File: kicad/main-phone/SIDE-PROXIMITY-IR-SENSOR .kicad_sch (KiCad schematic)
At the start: 1 part

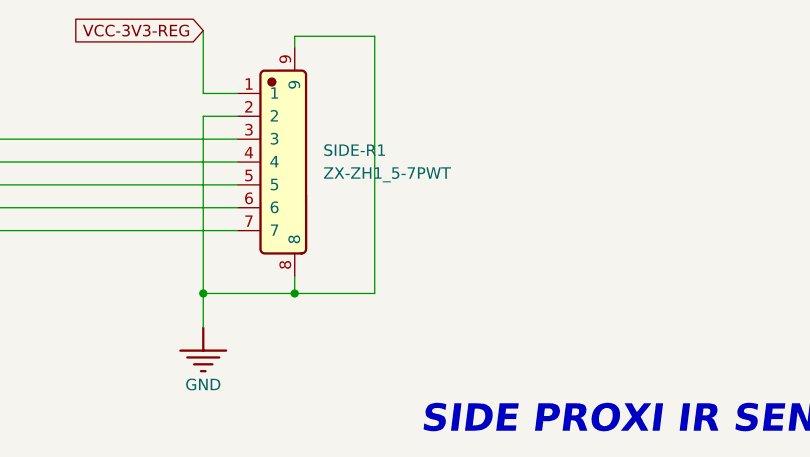
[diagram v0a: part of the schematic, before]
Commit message: Side sensor board rev 2 (VL53L0X + IRM-H638T, JST SH); mounting holes on dock and sensor boards
- kicad/side-sensors: VL53L0X (C91199) replaces the NRND VL6180 and its 2.8 V LDO;
  top-looking IRM-H638T replaces the TSOP38238; ZX-SH1.0-7PWT connector, same pinout;
  10k XSHUT/GPIO1 pull-ups, no local I2C pull-ups; refs 84xx; libs from ../main
- main-phone SIDE-R1: ZX-ZH1.5-7PWT -> ZX-SH1.0-7PWT
- mounting holes: dock 4x M3 (H8201-H8204), ToF board 2x M2 (H8301/H8302),
  side board 2x M2 (H8401/H8402)
- JLCImport: VL53L0CXV0DH_1 symbol, footprint, 3D model
- docs: side board README, SPEC, READMEs; IRM-H638T pinout confirmed

Co-Authored-By: Claude Opus 5.5 (1M context) <noreply@anthropic.com>
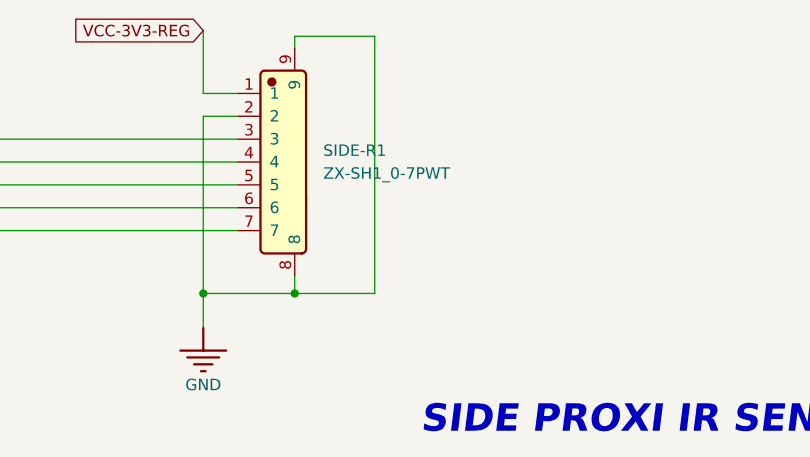
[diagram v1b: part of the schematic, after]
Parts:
- SIDE-R1: value ZX-ZH1_5-7PWT -> ZX-SH1_0-7PWT; footprint JLCImport:ZX-ZH1_5-7PWT -> JLCImport:ZX-SH1_0-7PWT; symbol JLCImport:ZX-ZH1_5-7PWT -> JLCImport:ZX-SH1_0-7PWT; LCSC C19272410 -> C7430449; Manufacturer Part ZX-ZH1.5-7PWT -> ZX-SH1.0-7PWT
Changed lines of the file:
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@@
 	)
 	(symbol
-		(lib_id "JLCImport:ZX-ZH1_5-7PWT")
+		(lib_id "JLCImport:ZX-SH1_0-7PWT")
 		(at 134.62 80.01 0)
 		(unit 1)
@@
 			)
 		)
-		(property "Value" "ZX-ZH1_5-7PWT"
+		(property "Value" "ZX-SH1_0-7PWT"
 			(at 139.065 81.2799 0)
 			(show_name no)
@@
 			)
 		)
-		(property "Footprint" "JLCImport:ZX-ZH1_5-7PWT"
+		(property "Footprint" "JLCImport:ZX-SH1_0-7PWT"
 			(at 134.62 80.01 0)
 			(hide yes)
@@
 			)
 		)
-		(property "Datasheet" "https://wmsc.lcsc.com/wmsc/upload/file/pdf/v2/lcsc/2312011606_Megastar-ZX-ZH1-5-7PWT_C19272410.pdf"
+		(property "Datasheet" "https://www.lcsc.com/datasheet/C7430449.pdf"
 			(at 134.62 80.01 0)
 			(hide yes)
@@
 			)
 		)
-		(property "Description" "-25℃~+85℃ 1 1.5mm 13.5mm 1A 1x7P 250V 3.8mm 6mm 7 7P Auxiliary Solder Pin Beige Brass LCP Surface Mount, Right Angle Tin ZH SMD,P=1.5mm,卧贴 Wire To Board Connector ROHS"
+		(property "Description" "JST SH compatible 1.0 mm 1x7P, SMD right angle; to the side sensor board (J8401)"
 			(at 134.62 80.01 0)
 			(hide yes)
@@
 			)
 		)
-		(property "LCSC" "C19272410"
+		(property "LCSC" "C7430449"
 			(at 134.62 80.01 0)
 			(hide yes)
@@
 			)
 		)
-		(property "Manufacturer Part" "ZX-ZH1.5-7PWT"
+		(property "Manufacturer Part" "ZX-SH1.0-7PWT"
 			(at 134.62 80.01 0)
 			(hide yes)

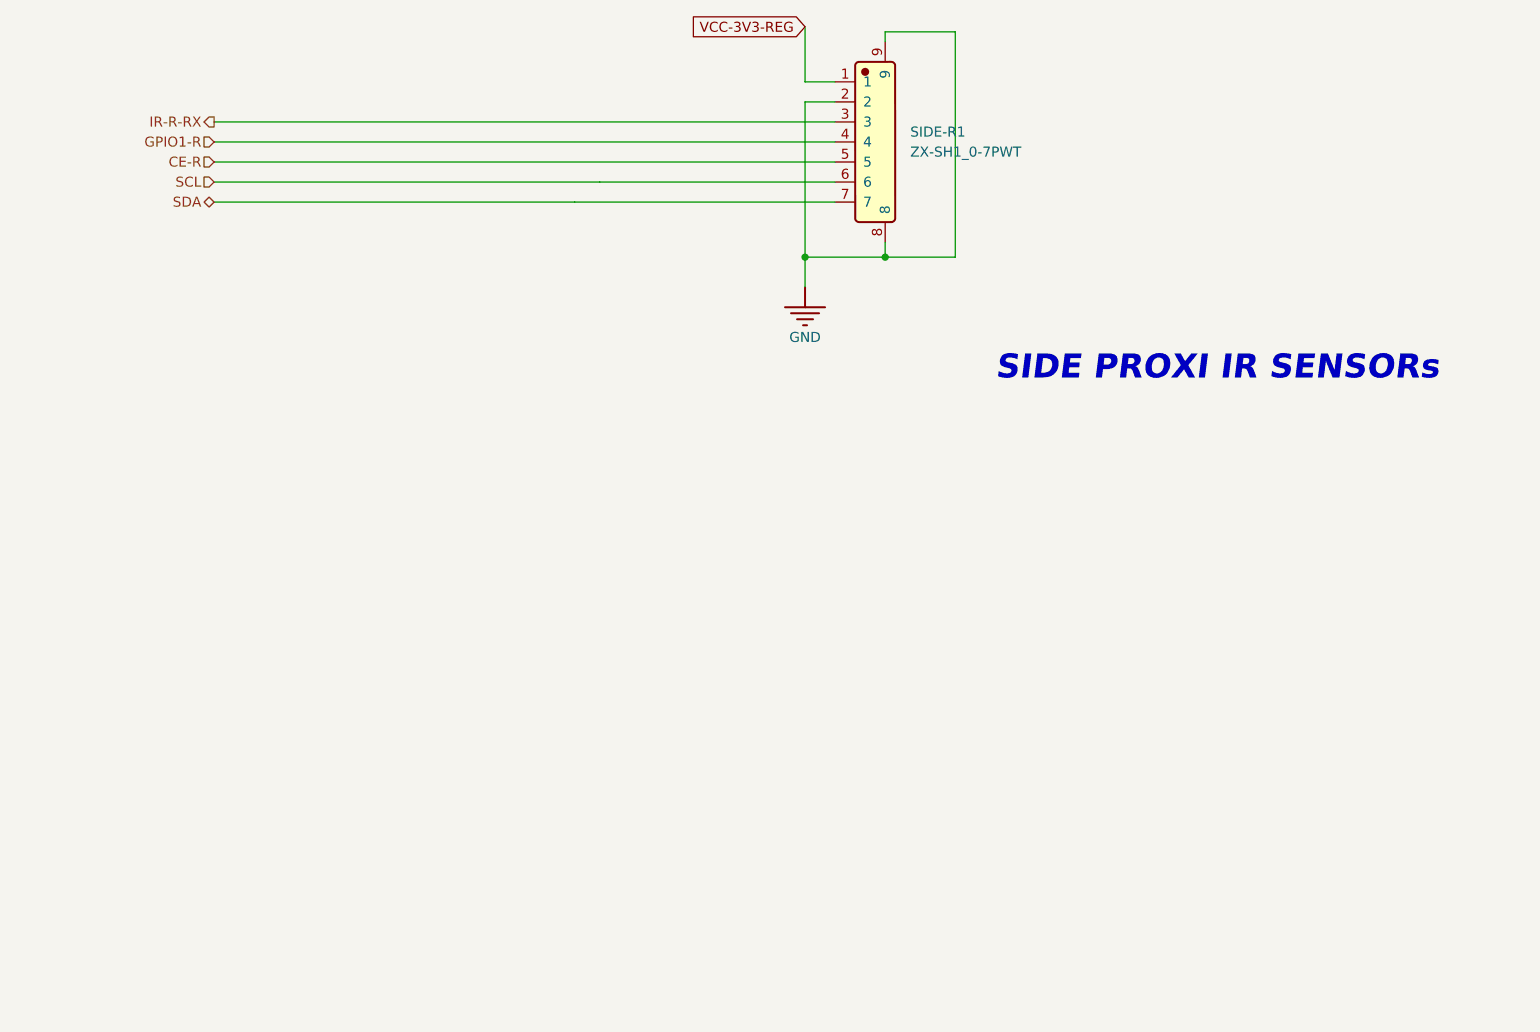
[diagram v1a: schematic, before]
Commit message: Rear docking IR board and Hall sensor board; main-board connectors
- kicad/rear-ir: 2x top-looking IRM-H638T with per-receiver 100R + 10uF filters, SH 4-pin
  vertical (3.3 V, IR_L, IR_R, GND), 2x M2. Refs 86xx.
- kicad/hall-sensor: CC6201ST omnipolar Hall switch + 100 nF, SH 4-pin vertical, 2x M2;
  fitted twice (dust bin, LiDAR tower bumper). Refs 87xx.
- main-phone SIDE-PROXI sheet: REAR-IR1 (PC8/PC9), HALL-BIN1 (PE4), HALL-TOWER1 (PE5),
  47k Hall pull-ups R7801/R7802; global labels to the MCU sheet; J7301 labels updated
- JLCImport: CC6201ST
- docs: board READMEs, SPEC, READMEs

Co-Authored-By: Claude Opus 5.5 <noreply@anthropic.com>
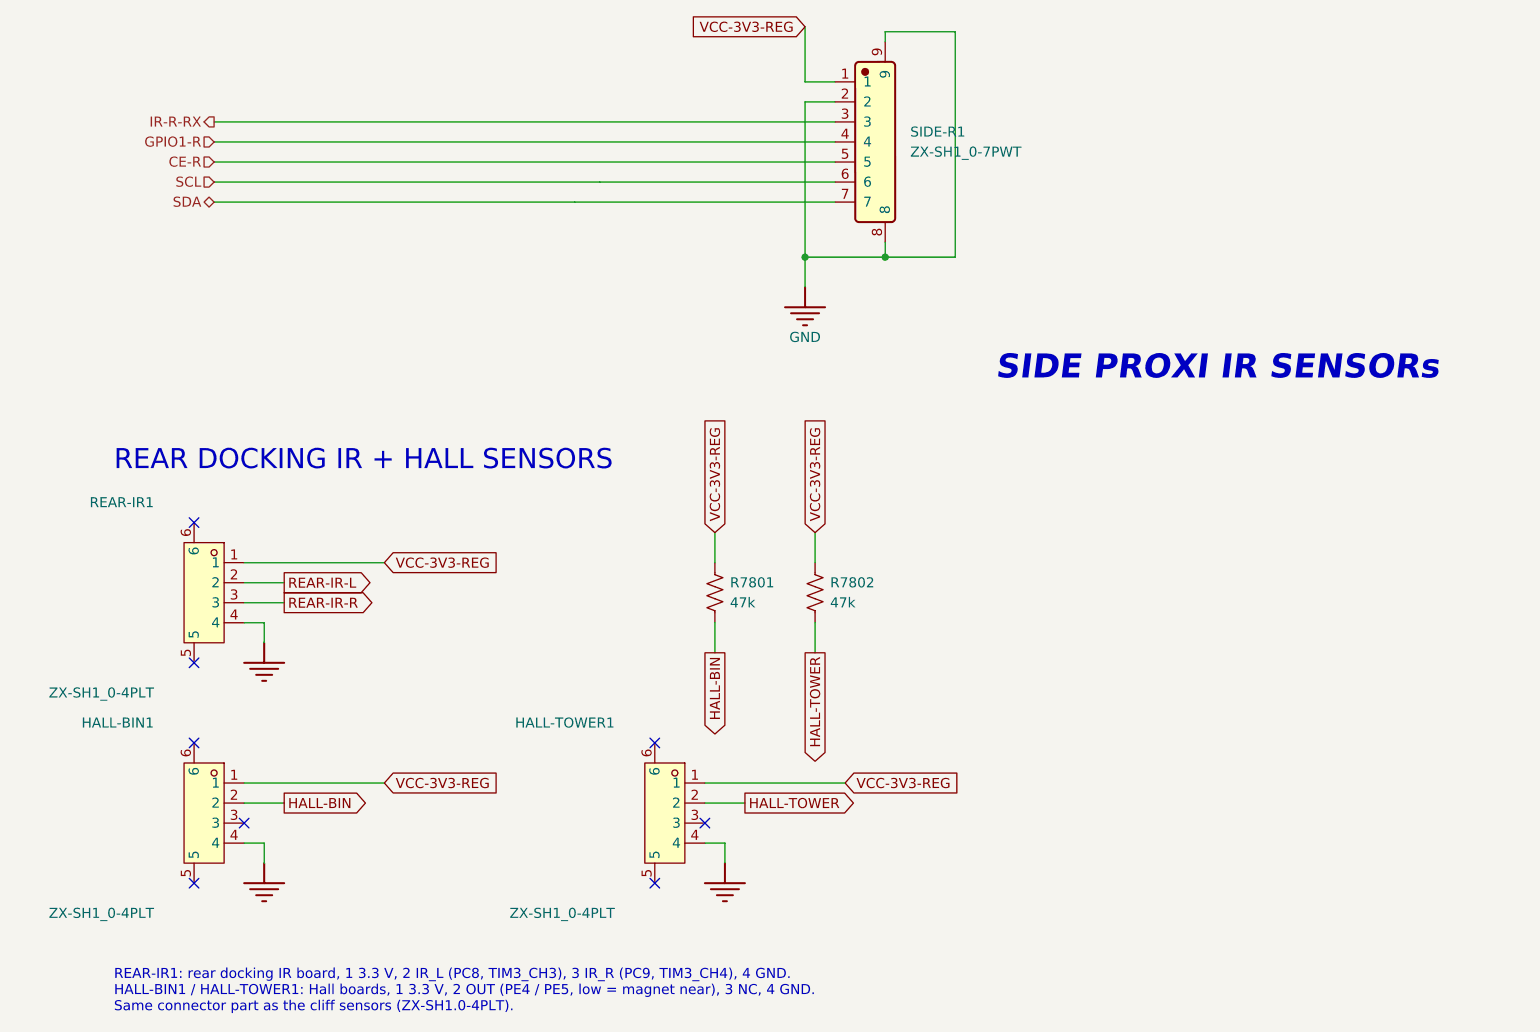
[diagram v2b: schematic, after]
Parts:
- added HALL-BIN1, HALL-TOWER1, REAR-IR1: ZX-SH1_0-4PLT, JLCImport:ZX-SH1_0-4PLT, symbol JLCImport:ZX-SH1_0-4PLT
- added R7801, R7802: 47k, Resistor_SMD:R_0603_1608Metric, symbol Device:R_US
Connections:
- net GND: now also HALL-BIN1.4, HALL-TOWER1.4, REAR-IR1.4
- net VCC-3V3-REG: now also HALL-BIN1.1, HALL-TOWER1.1, R7801.1, R7802.1, REAR-IR1.1
- new net HALL-BIN: HALL-BIN1.2, R7801.2
- new net HALL-TOWER: HALL-TOWER1.2, R7802.2
- new net REAR-IR-L: REAR-IR1.2
- new net REAR-IR-R: REAR-IR1.3
- no-connect marks 0 -> 8
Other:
- note added: "REAR DOCKING IR + HALL SENSORS"
- note added: "REAR-IR1: rear docking IR board, 1 3.3 V, 2 IR_L (PC8, TIM3_CH3), 3 IR_R (PC9, TIM3_CH4), 4 GND. HALL-BIN1 / HALL-TOWER1: Hall boards, 1 3.3 V, 2 OUT (PE4 / PE5, low = magnet near), 3 NC, 4 GND. Same connector part as the cliff sensors (ZX-SH1.0-4PLT)."
